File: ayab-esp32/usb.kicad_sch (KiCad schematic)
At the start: 6 parts, among them J601 USB_C_Receptacle_USB2.0, U601 SRV05-4

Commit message: first draft schematic
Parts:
- gave numbers to parts that had none: 2
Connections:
- net USB_5V renamed USB_VBUS
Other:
- company: matei repair lab -> matei
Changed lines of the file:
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@@
   (title_block
     (title "USB & ESD")
-    (date "2023-06-17")
-    (rev "1.0")
-    (company "matei repair lab")
+    (date "2023-07-17")
+    (rev "0.1")
+    (company "matei")
+    (comment 1 "ayab-knitting.com")
+    (comment 2 "distributed under CC-BY-SA-4.0")
   )
   (junction (at 133.35 86.36) (diameter 0) (color 0 0 0 0)
@@
   )
   (junction (at 182.88 74.93) (diameter 0) (color 0 0 0 0)
+  )
+  (junction (at 147.32 74.93) (diameter 0) (color 0 0 0 0)
   )
   (junction (at 149.86 88.9) (diameter 0) (color 0 0 0 0)
@@
     (stroke (width 0) (type default))
   )
+  (wire (pts (xy 147.32 74.93) (xy 171.45 74.93))
+    (stroke (width 0) (type default))
+  )
   (wire (pts (xy 149.86 105.41) (xy 160.02 105.41))
     (stroke (width 0) (type default))
@@
     (stroke (width 0) (type default))
   )
+  (wire (pts (xy 151.13 69.85) (xy 147.32 69.85))
+    (stroke (width 0) (type default))
+  )
+  (wire (pts (xy 147.32 69.85) (xy 147.32 74.93))
+    (stroke (width 0) (type default))
+  )
   (wire (pts (xy 129.54 80.01) (xy 135.89 80.01))
     (stroke (width 0) (type default))
@@
     (stroke (width 0) (type default))
   )
-  (wire (pts (xy 129.54 74.93) (xy 171.45 74.93))
+  (wire (pts (xy 129.54 74.93) (xy 147.32 74.93))
     (stroke (width 0) (type default))
   )
@@
   (wire (pts (xy 160.02 80.01) (xy 160.02 81.28))
     (stroke (width 0) (type default))
-  )
-  (label "USB_5V" (at 151.13 74.93 0) (fields_autoplaced)
-    (effects (font (size 1.27 1.27)) (justify left bottom))
   )
   (hierarchical_label "USB_M" (shape bidirectional) (at 135.89 86.36 0) (fields_autoplaced)
@@
   )
   (hierarchical_label "UCPD_CC2" (shape bidirectional) (at 135.89 82.55 0) (fields_autoplaced)
+    (effects (font (size 1.27 1.27)) (justify left))
+  )
+  (hierarchical_label "USB_VBUS" (shape output) (at 151.13 69.85 0) (fields_autoplaced)
     (effects (font (size 1.27 1.27)) (justify left))
   )
@@
   (symbol (lib_id "Device:C_Small") (at 160.02 100.33 0) (unit 1)
     (in_bom yes) (on_board yes) (dnp no)
-    (property "Reference" "C?" (at 157.48 99.0663 0)
+    (property "Reference" "C202" (at 157.48 99.0663 0)
       (effects (font (size 1.27 1.27)) (justify right))
     )
@@
       (project "ayab-esp32"
         (path "/ad16b75f-afc8-4717-a7c6-8dd7b69a18e2/7889acbf-96cc-4a04-a98d-615c06d1b134"
-          (reference "C?") (unit 1)
+          (reference "C202") (unit 1)
         )
       )
@@
   (symbol (lib_id "power:GND") (at 160.02 107.95 0) (mirror y) (unit 1)
     (in_bom yes) (on_board yes) (dnp no)
-    (property "Reference" "#PWR?" (at 160.02 114.3 0)
+    (property "Reference" "#PWR0107" (at 160.02 114.3 0)
       (effects (font (size 1.27 1.27)) hide)
     )
@@
       (project "ayab-esp32"
         (path "/ad16b75f-afc8-4717-a7c6-8dd7b69a18e2/7889acbf-96cc-4a04-a98d-615c06d1b134"
-          (reference "#PWR?") (unit 1)
+          (reference "#PWR0107") (unit 1)
         )
       )
@@
   (symbol (lib_id "Device:C_Small") (at 149.86 100.33 0) (unit 1)
     (in_bom yes) (on_board yes) (dnp no)
-    (property "Reference" "C?" (at 147.32 99.0663 0)
+    (property "Reference" "C201" (at 147.32 99.0663 0)
       (effects (font (size 1.27 1.27)) (justify right))
     )
@@
       (project "ayab-esp32"
         (path "/ad16b75f-afc8-4717-a7c6-8dd7b69a18e2/7889acbf-96cc-4a04-a98d-615c06d1b134"
-          (reference "C?") (unit 1)
-        )
-      )
+          (reference "C201") (unit 1)
+        )
+      )

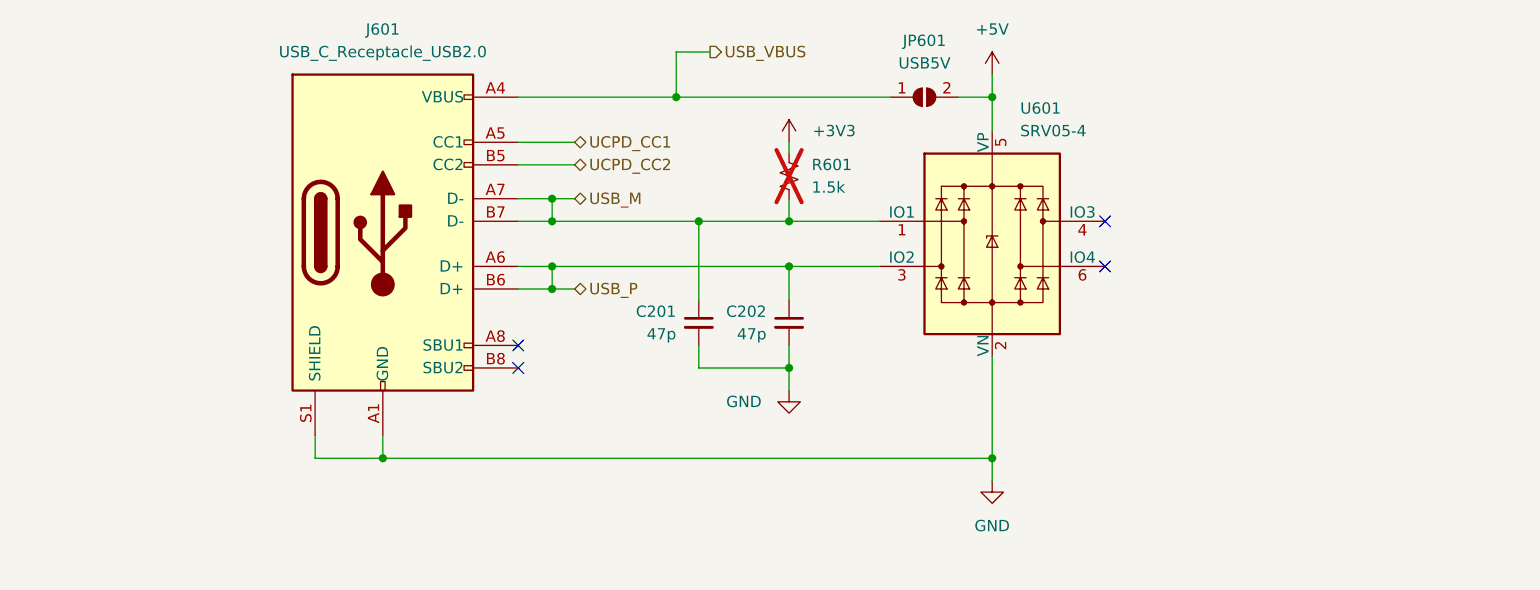
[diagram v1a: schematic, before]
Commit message: add ideal diode, remove extra uln2003a, add comparator for analog EOL sensors
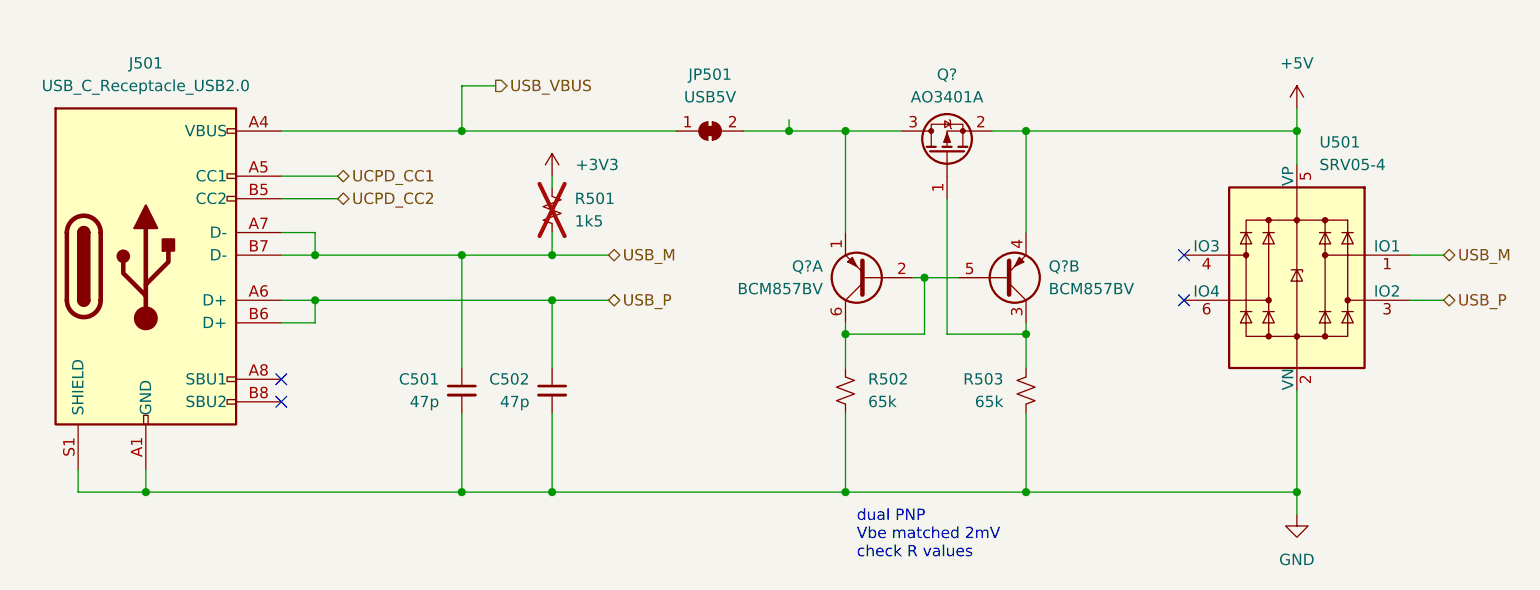
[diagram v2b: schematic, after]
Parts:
- added Q? (x2): BCM857BV, symbol Device:Q_Dual_PNP_PNP_E1B1C2E2B2C1
- added Q?: AO3401A, Package_TO_SOT_SMD:SOT-23, symbol Transistor_FET:AO3401A
- added R502, R503: 65k, symbol Device:R_Small_US
- JP501: renamed from JP601; symbol Jumper:SolderJumper_2_Open -> Jumper:SolderJumper_2_Bridged
- R501: renamed from R601; value 1.5k -> 1k5
- renumbered C201 to C501, C202 to C502, J601 to J501, U601 to U501
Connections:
- net +5V: now also Q?.2 (S), Q?.4 (E2); no longer JP501.2 (B)
- net GND: now also R502.2, R503.2
- new net: Q?.1 (G), Q?.3 (C2), R503.1
- new net: JP501.2 (B), Q?.1 (E1), Q?.3 (D)
- new net: Q?.2 (B1), Q?.5 (B2), Q?.6 (C1), R502.1
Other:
- note added: "dual PNP Vbe matched 2mV check R values"
- moved on the sheet: C501, C502, J501, R501, U501

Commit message: fix folder structure and update gitignore
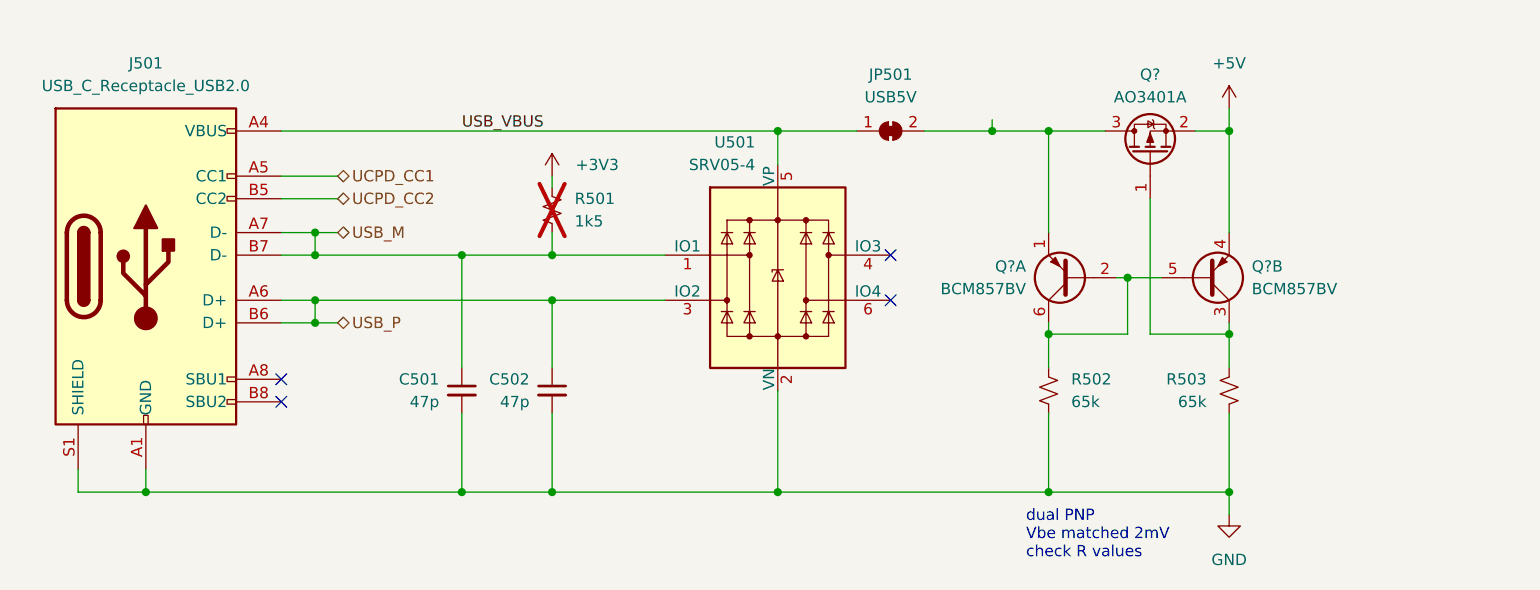
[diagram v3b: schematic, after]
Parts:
- removed U501: SRV05-4, Package_TO_SOT_SMD:SOT-23-6, symbol Power_Protection:SRV05-4
- added U501: SRV05-4, Package_TO_SOT_SMD:SOT-23-6, symbol ayab-esp32:SRV05-4
- C501, C502: symbol Device:C_Small -> ayab-esp32:C_Small
- J501: symbol Connector:USB_C_Receptacle_USB2.0 -> ayab-esp32:USB_C_Receptacle_USB2.0
- JP501: symbol Jumper:SolderJumper_2_Bridged -> ayab-esp32:SolderJumper_2_Bridged
- Q? (x2): symbol Device:Q_Dual_PNP_PNP_E1B1C2E2B2C1 -> ayab-esp32:Q_Dual_PNP_PNP_E1B1C2E2B2C1
- Q?: symbol Transistor_FET:AO3401A -> ayab-esp32:AO3401A
- R501, R502, R503: symbol Device:R_Small_US -> ayab-esp32:R_Small_US
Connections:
- net GND: now also U501.2 (VN)
- net USB_M: now also U501.1 (IO1)
- net USB_P: now also U501.3 (IO2)
- net USB_VBUS: now also U501.5 (VP)
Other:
- moved on the sheet: JP501, Q?, Q?A, Q?B, R502, R503

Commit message: add component selection, bom
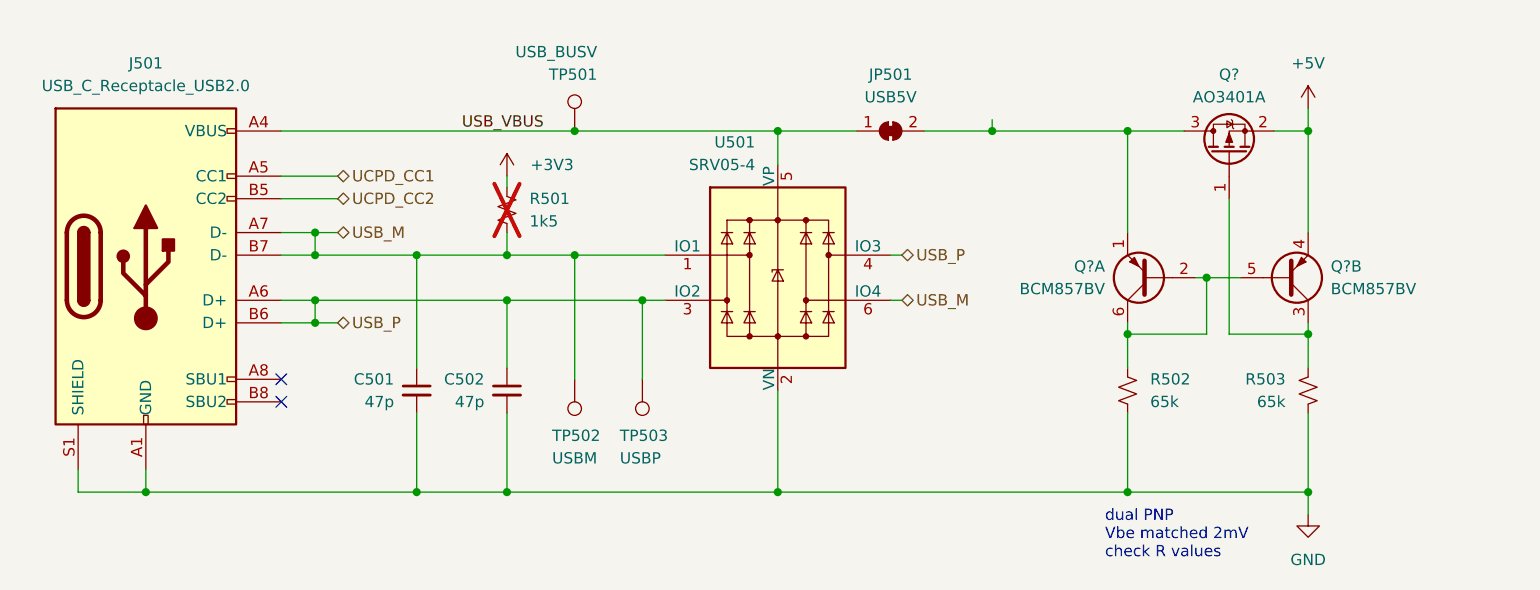
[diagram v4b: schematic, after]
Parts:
- added TP501: USB_BUSV, TestPoint:TestPoint_Pad_D2.0mm, symbol Library:TestPoint
- added TP502: USBM, TestPoint:TestPoint_Pad_D2.0mm, symbol Library:TestPoint
- added TP503: USBP, TestPoint:TestPoint_Pad_D2.0mm, symbol Library:TestPoint
- C501, C502: footprint Capacitor_SMD:C_0402_1005Metric -> Capacitor_SMD:C_0603_1608Metric; symbol ayab-esp32:C_Small -> Library:C_Small; LCSC ID (none) -> C1671; OEM (none) -> Samsung Electro-Mechanics; OEM PN (none) -> CL10C470JB8NNNC; Package (none) -> 0603; Voltage rating (none) -> 50V C0G
- J501: symbol ayab-esp32:USB_C_Receptacle_USB2.0 -> Library:USB_C_Receptacle_USB2.0; LCSC ID (none) -> C165948; OEM (none) -> Hroparts; OEM PN (none) -> TYPE-C-31-M-12
- JP501: symbol ayab-esp32:SolderJumper_2_Bridged -> Library:SolderJumper_2_Bridged
- Q? (x2): footprint (none) -> Package_TO_SOT_SMD:SOT-363_SC-70-6; symbol ayab-esp32:Q_Dual_PNP_PNP_E1B1C2E2B2C1 -> Library:Q_Dual_PNP_PNP_E1B1C2E2B2C1; LCSC ID (none) -> C105887; OEM (none) -> Nexperia; OEM PN (none) -> BCM857BS,115; Package (none) -> SOT-363
- Q?: symbol ayab-esp32:AO3401A -> Library:AO3401A; LCSC ID (none) -> C15127; OEM (none) -> Alpha & Omega Semicon; OEM PN (none) -> AO3401A; Package (none) -> SOT-23
- R501: footprint Resistor_SMD:R_0402_1005Metric -> Resistor_SMD:R_0603_1608Metric; symbol ayab-esp32:R_Small_US -> Library:R_Small_US; LCSC ID (none) -> C22843; OEM (none) -> UNI-ROYAL(Uniroyal Elec); OEM PN (none) -> 0603WAF1501T5E; Package (none) -> 0603
- R502, R503: footprint (none) -> Resistor_SMD:R_0603_1608Metric; symbol ayab-esp32:R_Small_US -> Library:R_Small_US; LCSC ID (none) -> check values; Package (none) -> 0603
- U501: symbol ayab-esp32:SRV05-4 -> Library:SRV05-4; LCSC ID (none) -> C7420376; OEM (none) -> hongjiacheng; OEM PN (none) -> SRV05-4; Package (none) -> SOT-23-6
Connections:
- net USB_M: now also U501.6 (IO4), TP502.1
- net USB_P: now also U501.4 (IO3), TP503.1
- net USB_VBUS: now also TP501.1
- no-connect marks 4 -> 2
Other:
- moved on the sheet: C501, C502, Q?, Q?A, Q?B, R501, R502, R503

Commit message: review ZVD P-ch MOSFET and resistors
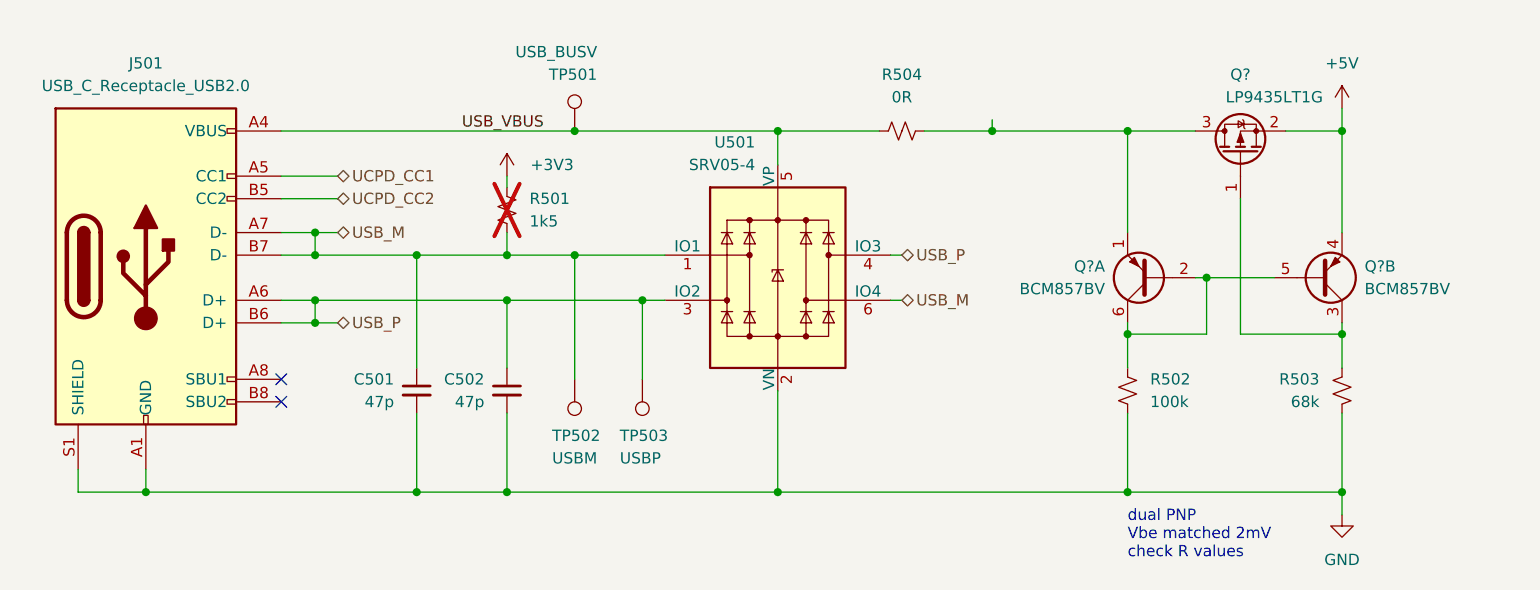
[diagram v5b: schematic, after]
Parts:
- removed JP501: USB5V, Jumper:SolderJumper-2_P1.3mm_Bridged_RoundedPad1.0x1.5mm, symbol Library:SolderJumper_2_Bridged
- added R504: 0R, Resistor_SMD:R_0603_1608Metric, symbol ayab-lib:R_Small_US
- C501, C502: symbol Library:C_Small -> ayab-lib:C_Small
- J501: symbol Library:USB_C_Receptacle_USB2.0 -> ayab-lib:USB_C_Receptacle_USB2.0
- Q? (x2): symbol Library:Q_Dual_PNP_PNP_E1B1C2E2B2C1 -> ayab-lib:Q_Dual_PNP_PNP_E1B1C2E2B2C1
- Q?: value AO3401A -> LP9435LT1G; symbol Library:AO3401A -> ayab-lib:AO3401A; LCSC ID C15127 -> C383257; OEM Alpha & Omega Semicon -> LRC; OEM PN AO3401A -> LP9435LT1G; Voltage rating (none) -> 30V
- R501: symbol Library:R_Small_US -> ayab-lib:R_Small_US
- R502: value 65k -> 100k; symbol Library:R_Small_US -> ayab-lib:R_Small_US; LCSC ID check values -> C25803; OEM (none) -> UNI-ROYAL(Uniroyal Elec); OEM PN (none) -> 0603WAF1003T5E
- R503: value 65k -> 68k; symbol Library:R_Small_US -> ayab-lib:R_Small_US; LCSC ID check values -> C23231; OEM (none) -> UNI-ROYAL(Uniroyal Elec); OEM PN (none) -> 0603WAF6802T5E
- TP501, TP502, TP503: symbol Library:TestPoint -> ayab-lib:TestPoint
- U501: symbol Library:SRV05-4 -> ayab-lib:SRV05-4
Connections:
- net USB_VBUS: now also R504.1
- net at Q?.1 (E1), Q?.3 (D): now also R504.2
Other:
- moved on the sheet: Q?, Q?B, R503

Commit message: first draft layout DRC clean
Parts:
- TP501, TP502, TP503: footprint TestPoint:TestPoint_Pad_D2.0mm -> TestPoint:TestPoint_Pad_D1.0mm
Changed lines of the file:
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@@
       (effects (font (size 1.27 1.27)) (justify right))
     )
-    (property "Footprint" "TestPoint:TestPoint_Pad_D2.0mm" (at 138.43 106.68 0)
+    (property "Footprint" "TestPoint:TestPoint_Pad_D1.0mm" (at 138.43 106.68 0)
       (effects (font (size 1.27 1.27)) hide)
     )
@@
       (effects (font (size 1.27 1.27)) (justify right))
     )
-    (property "Footprint" "TestPoint:TestPoint_Pad_D2.0mm" (at 140.97 78.74 0)
+    (property "Footprint" "TestPoint:TestPoint_Pad_D1.0mm" (at 140.97 78.74 0)
       (effects (font (size 1.27 1.27)) hide)
     )
@@
       (effects (font (size 1.27 1.27)) (justify right))
     )
-    (property "Footprint" "TestPoint:TestPoint_Pad_D2.0mm" (at 130.81 106.68 0)
-      (effects (font (size 1.27 1.27)) hide)
-    )
+    (property "Footprint" "TestPoint:TestPoint_Pad_D1.0mm" (at 130.81 106.68 0)
+      (effects (font (size 1.27 1.27)) hide)
+    )

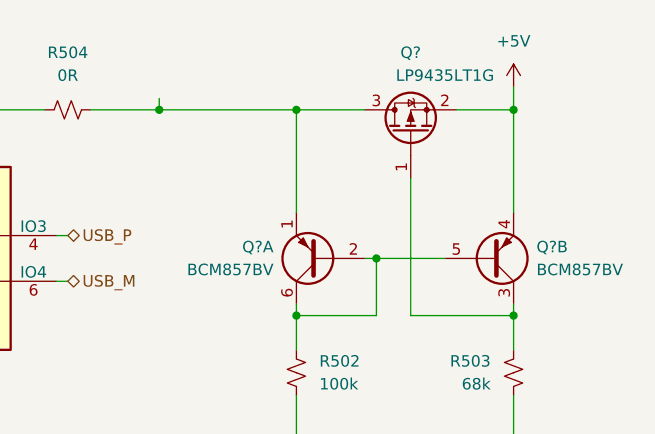
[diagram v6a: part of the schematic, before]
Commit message: revise connector positions
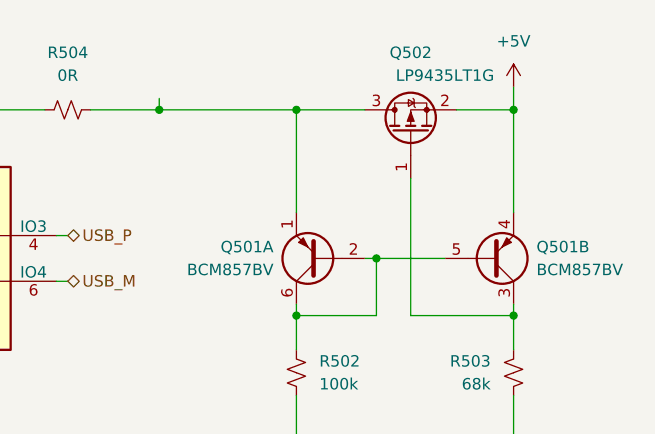
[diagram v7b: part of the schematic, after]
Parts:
- gave numbers to parts that had none: 2
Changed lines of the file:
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@@
   (symbol (lib_id "ayab-lib:Q_Dual_PNP_PNP_E1B1C2E2B2C1") (at 200.66 95.25 180) (unit 1)
     (in_bom yes) (on_board yes) (dnp no)
-    (property "Reference" "Q?" (at 195.58 93.98 0)
+    (property "Reference" "Q501" (at 195.58 93.98 0)
       (effects (font (size 1.27 1.27)) (justify left))
     )
@@
     (instances
       (project "ayab-esp32"
-        (path "/ad16b75f-afc8-4717-a7c6-8dd7b69a18e2/512b1de4-f8f4-4173-a7be-69b46f59a5e5"
-          (reference "Q?") (unit 1)
-        )
         (path "/ad16b75f-afc8-4717-a7c6-8dd7b69a18e2/7889acbf-96cc-4a04-a98d-615c06d1b134"
           (reference "Q501") (unit 1)
@@
   (symbol (lib_id "ayab-lib:AO3401A") (at 210.82 81.28 90) (unit 1)
     (in_bom yes) (on_board yes) (dnp no)
-    (property "Reference" "Q?" (at 210.82 72.39 90)
+    (property "Reference" "Q502" (at 210.82 72.39 90)
       (effects (font (size 1.27 1.27)))
     )
@@
     (instances
       (project "ayab-esp32"
-        (path "/ad16b75f-afc8-4717-a7c6-8dd7b69a18e2/512b1de4-f8f4-4173-a7be-69b46f59a5e5"
-          (reference "Q?") (unit 1)
-        )
         (path "/ad16b75f-afc8-4717-a7c6-8dd7b69a18e2/7889acbf-96cc-4a04-a98d-615c06d1b134"
           (reference "Q502") (unit 1)
@@
   (symbol (lib_id "ayab-lib:Q_Dual_PNP_PNP_E1B1C2E2B2C1") (at 219.71 95.25 0) (mirror x) (unit 2)
     (in_bom yes) (on_board yes) (dnp no) (fields_autoplaced)
-    (property "Reference" "Q?" (at 224.79 93.98 0)
+    (property "Reference" "Q501" (at 224.79 93.98 0)
       (effects (font (size 1.27 1.27)) (justify left))
     )
@@
     (instances
       (project "ayab-esp32"
-        (path "/ad16b75f-afc8-4717-a7c6-8dd7b69a18e2/512b1de4-f8f4-4173-a7be-69b46f59a5e5"
-          (reference "Q?") (unit 2)
-        )
         (path "/ad16b75f-afc8-4717-a7c6-8dd7b69a18e2/7889acbf-96cc-4a04-a98d-615c06d1b134"
           (reference "Q501") (unit 2)

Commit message: add mouser parts list
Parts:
- C501, C502: Mouser PN (none) -> 80-C0603C470G3HACTU
- J501: Mouser PN (none) -> 640-USB4105-GF-A
- Q501: Mouser PN (none) -> 771-BCM857BV,115
- R501: Mouser PN (none) -> 708-RMCF0603JT1K50
- R502: Mouser PN (none) -> 71-CRCW0603100KJNEAC
- R503: Mouser PN (none) -> 603-RC0603FR-1068KL
- R504: Mouser PN (none) -> 71-CRCW06030000Z0EC
- U501: Mouser PN (none) -> 947-SRV05-4.TCT
